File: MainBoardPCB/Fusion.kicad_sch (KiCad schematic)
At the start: 14 parts, among them J2 Conn_02x20_Odd_Even, J5 Conn_02x16_Odd_Even, J7 Conn_02x08_Odd_Even

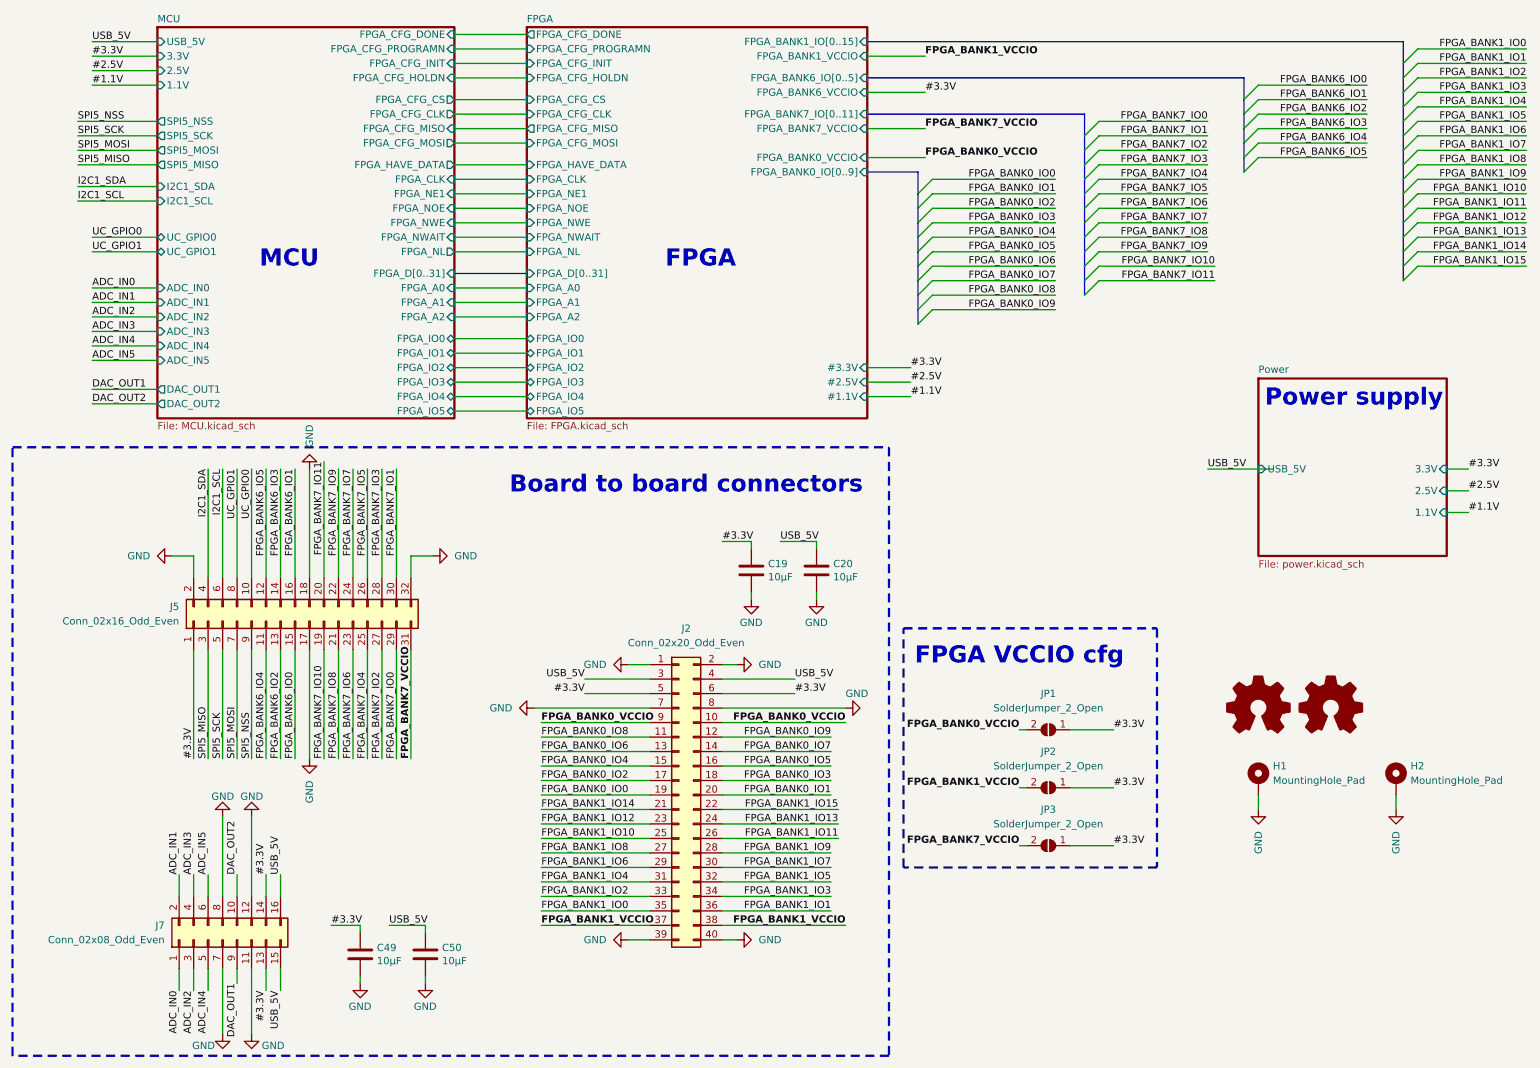
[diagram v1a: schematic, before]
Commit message: New Fusion main board version using a more beefy MCU.
Signed-off-by: Alexis Jeandet <alexis.jeandet@member.fsf.org>
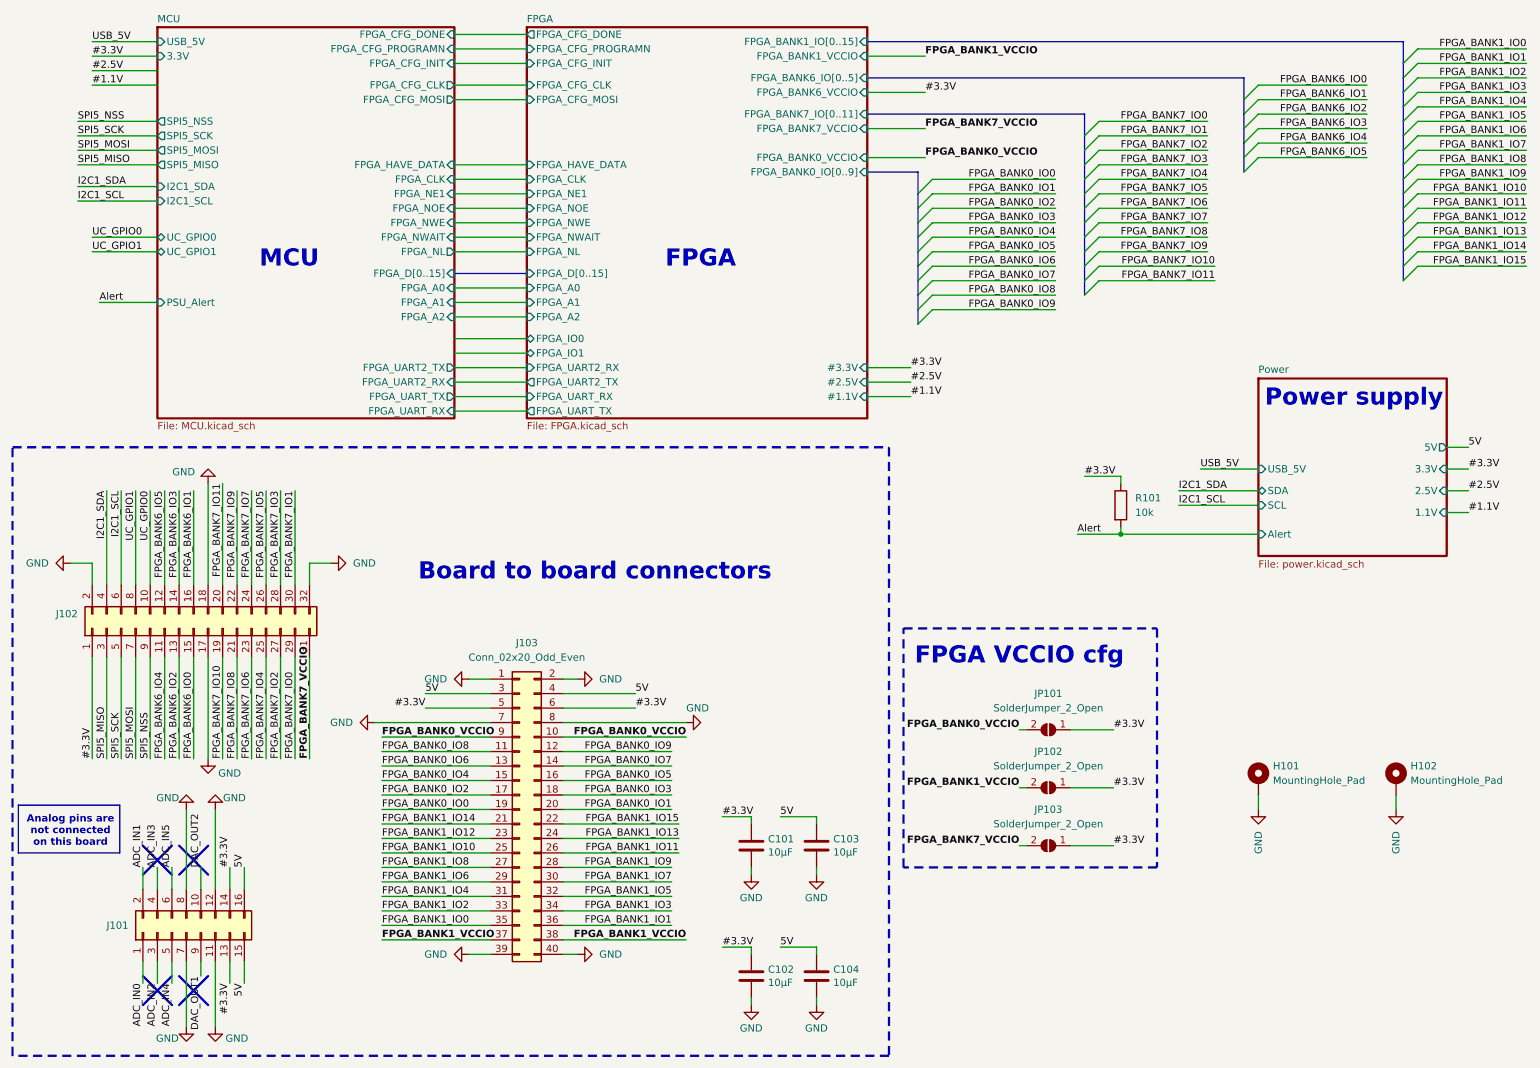
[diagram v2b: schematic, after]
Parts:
- removed SYM1: Logo_Open_Hardware_Small, Symbol:OSHW-Logo_11.4x12mm_SilkScreen, symbol Graphic:Logo_Open_Hardware_Small
- removed SYM2: Logo_Open_Hardware_Small, Symbol:KiCad-Logo2_8mm_SilkScreen, symbol Graphic:Logo_Open_Hardware_Small
- added R101: 10k, Capacitor_SMD:C_0603_1608Metric_Pad1.08x0.95mm_HandSolder, symbol Device:R
- renumbered C49 to C101, C19 to C102, C50 to C103, C20 to C104, H1 to H101, H2 to H102, J7 to J101, J5 to J102, J2 to J103, JP1 to JP101, JP2 to JP102, JP3 to JP103
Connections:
- net #3.3V: now also R101.1
- net USB_5V: no longer C103.1, C104.1, J101.15 (Pin_15), J101.16 (Pin_16), J103.3 (Pin_3), J103.4 (Pin_4)
- new net 5V: C103.1, C104.1, J101.15 (Pin_15), J101.16 (Pin_16), J103.3 (Pin_3), J103.4 (Pin_4)
- new net Alert: R101.2
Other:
- sheet FPGA ports: added FPGA_D[0..15], FPGA_UART2_RX, FPGA_UART2_TX, FPGA_UART_RX, FPGA_UART_TX; removed FPGA_CFG_CS, FPGA_CFG_HOLDN, FPGA_CFG_MISO, FPGA_D[0..31], FPGA_IO2, FPGA_IO3, FPGA_IO4, FPGA_IO5
- sheet MCU ports: added FPGA_D[0..15], FPGA_UART2_RX, FPGA_UART2_TX, FPGA_UART_RX, FPGA_UART_TX, PSU_Alert; removed 1.1V, 2.5V, ADC_IN0, ADC_IN1, ADC_IN2, ADC_IN3, ADC_IN4, ADC_IN5, DAC_OUT1, DAC_OUT2, FPGA_CFG_CS, FPGA_CFG_HOLDN, FPGA_CFG_MISO, FPGA_D[0..31], FPGA_IO0, FPGA_IO1, FPGA_IO2, FPGA_IO3, FPGA_IO4, FPGA_IO5
- sheet Power ports: added 5V, Alert, SCL, SDA; removed none
- note added: "Analog pins are not connected on this board"
- moved on the sheet: C101, C102, C103, C104, J101, J102, J103

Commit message: New FPGA only version
Signed-off-by: Alexis Jeandet <alexis.jeandet@member.fsf.org>
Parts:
- removed H101, H102: MountingHole_Pad, MountingHole:MountingHole_2.5mm_Pad, symbol Mechanical:MountingHole_Pad
- R101: footprint Capacitor_SMD:C_0603_1608Metric_Pad1.08x0.95mm_HandSolder -> Resistor_SMD:R_0402_1005Metric_Pad0.72x0.64mm_HandSolder
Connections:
- net #3.3V renamed 3.3V
- net I2C1_SCL renamed EXT_I²C.SCL
- net I2C1_SDA renamed EXT_I²C.SDA
- net SPI5_MISO renamed EXT_SPI.MISO
- net SPI5_MOSI renamed EXT_SPI.MOSI
- net SPI5_NSS renamed EXT_SPI.NSS
- net SPI5_SCK renamed EXT_SPI.SCK
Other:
- removed sheet MCU
- added sheet JTAG (JTAG.kicad_sch)
- added sheet RAM (RAM.kicad_sch)
- added sheet USB (USB.kicad_sch)
- sheet FPGA ports: added EXT_I²C{I²C}, EXT_SPI{SPI}, JTAG{JTAG}, SDRAM{SDRAM_ADDRESS}, SDRAM{SDRAM_CTRL}, SDRAM{SDRAM_DATA}, UART1{UART}, UART2{UART}, UC_GPIO0, UC_GPIO1, ULPI{CLKOUT RESET}, ULPI{ULPI_CTRL}, ULPI{ULPI_DATA}, {POWER}; removed #1.1V, #2.5V, #3.3V, FPGA_A0, FPGA_A1, FPGA_A2, FPGA_CFG_CLK, FPGA_CFG_DONE, FPGA_CFG_INIT, FPGA_CFG_MOSI, FPGA_CFG_PROGRAMN, FPGA_CLK, FPGA_D[0..15], FPGA_HAVE_DATA, FPGA_IO0, FPGA_IO1, FPGA_NE1, FPGA_NL, FPGA_NOE, FPGA_NWAIT, FPGA_NWE, FPGA_UART2_RX, FPGA_UART2_TX, FPGA_UART_RX, FPGA_UART_TX
- sheet Power ports: added {I²C}, {POWER}; removed 1.1V, 2.5V, 3.3V, 5V, SCL, SDA
- note added: "JTAG & HK"
- note added: "PSU Monitoring"
- note added: "SDRAM"
- note added: "USB"
- note removed: "MCU"
- moved on the sheet: C101, C102, C103, C104, J101, J102, J103, JP101, JP102, JP103, R101
